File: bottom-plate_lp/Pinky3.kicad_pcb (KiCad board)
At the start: 2 copper layers, 137 x 100.9 mm, 5 parts

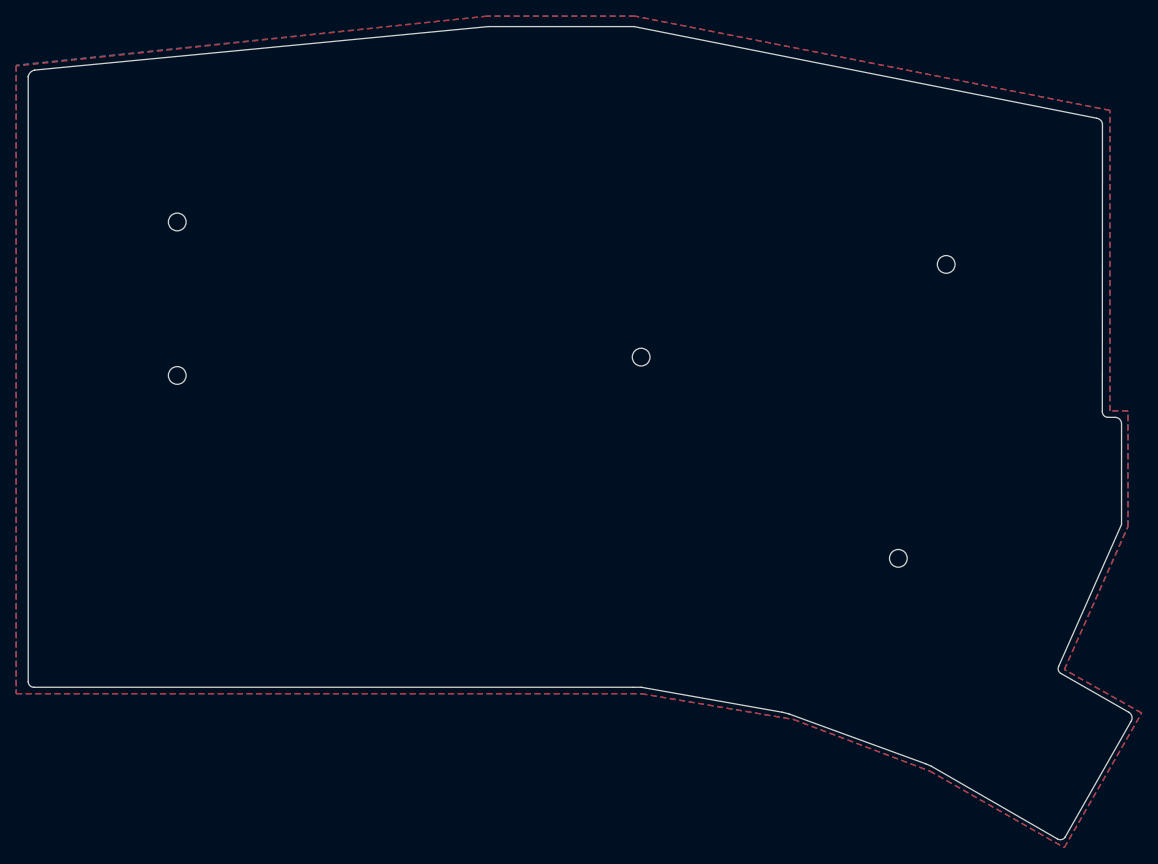
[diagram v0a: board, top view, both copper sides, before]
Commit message: update lp version for pcb, switchplate, bottom-plate
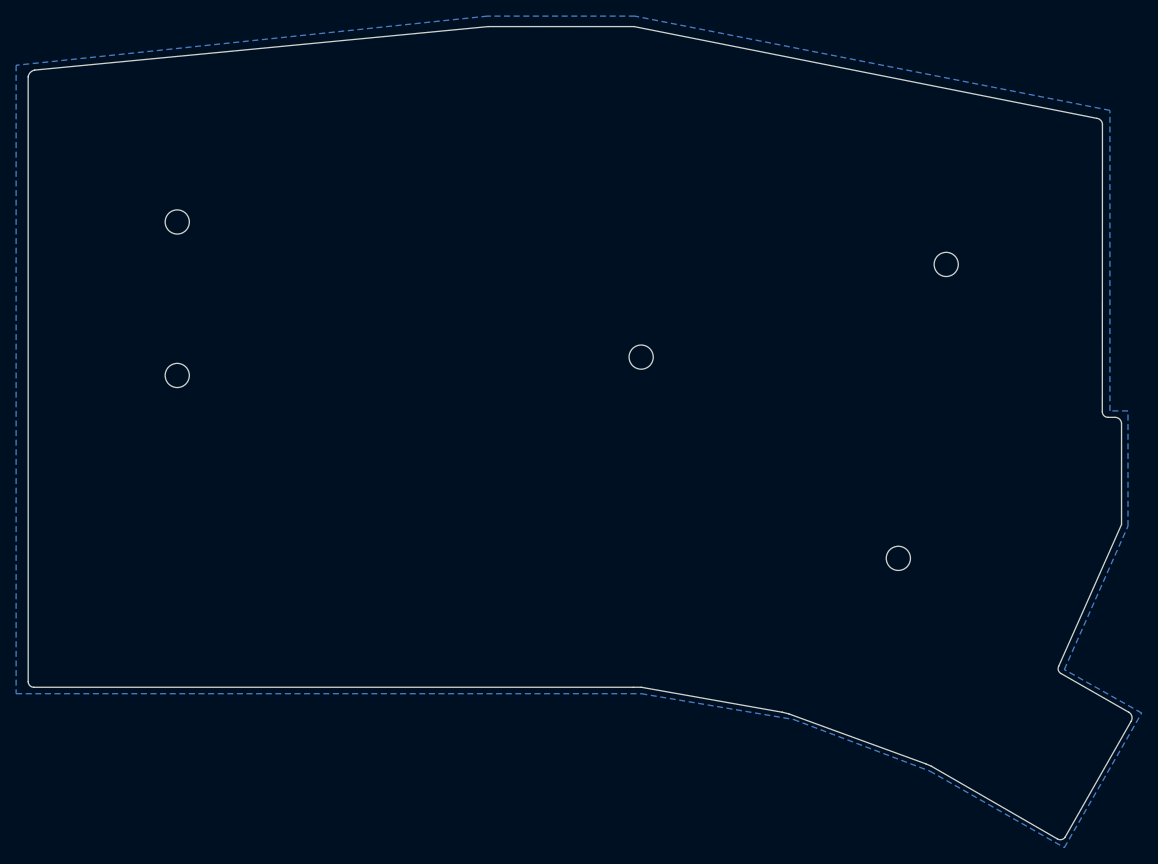
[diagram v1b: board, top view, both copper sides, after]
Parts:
- removed HOLE_M2 (x5): VAL**, kbd:HOLE_M2
- added Ref**: Val**, PCM_SparkFun-Hardware:Standoff_Reflow-M2.0, F.Cu at (59.5, 78.5)
- added Ref**: Val**, PCM_SparkFun-Hardware:Standoff_Reflow-M2.0, F.Cu at (59.5, 97.6)
- added Ref**: Val**, PCM_SparkFun-Hardware:Standoff_Reflow-M2.0, F.Cu at (117.1, 95.3)
- added Ref**: Val**, PCM_SparkFun-Hardware:Standoff_Reflow-M2.0, F.Cu at (154.9, 83.8)
- added Ref**: Val**, PCM_SparkFun-Hardware:Standoff_Reflow-M2.0, F.Cu at (149.0, 120.3)
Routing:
- removed copper zone on F.Cu, net GND
